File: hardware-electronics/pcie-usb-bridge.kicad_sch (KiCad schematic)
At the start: 27 parts, among them U10 24AA04T-I_OT, U3 PI7C9X440SLBFDE, Y1 ABM8-12.000MHZ-B2-T

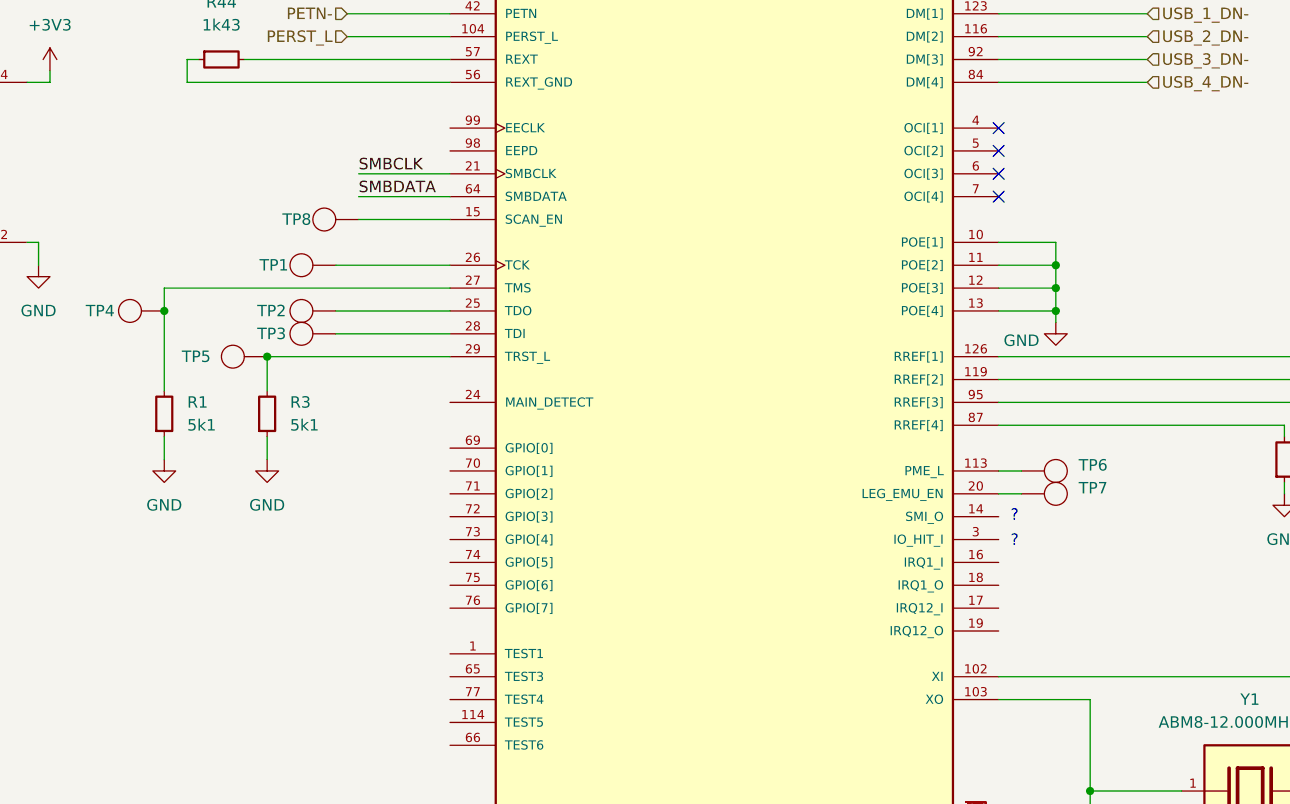
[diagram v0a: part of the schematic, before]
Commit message: [#8] SCH PCIe to USB Add TP to OHCI USB mode
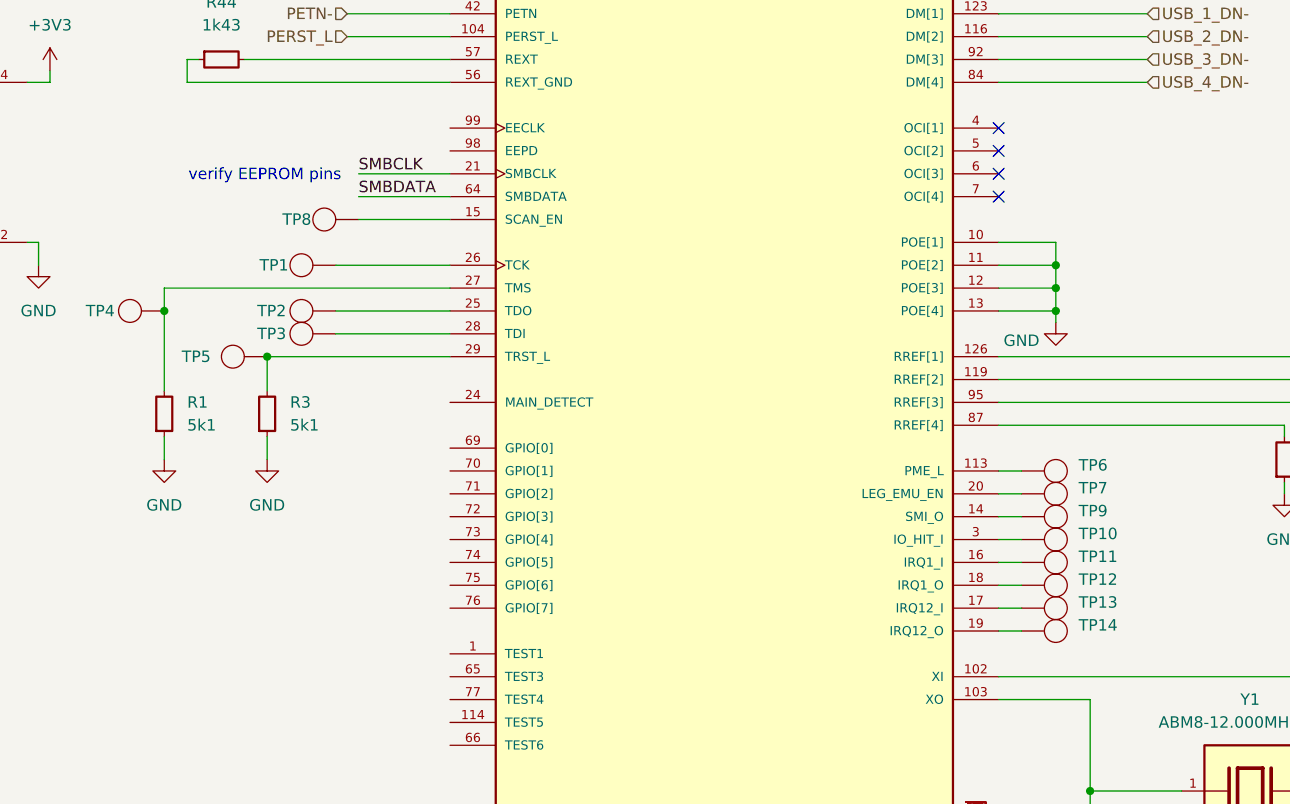
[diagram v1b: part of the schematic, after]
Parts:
- added TP10, TP11, TP12, TP13, TP14, TP9: ~, symbol M2SmartHomeSymbols:TP_SMD_1mm
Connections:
- net at U3.14 (SMI_O): now also TP9.
- net at U3.16 (IRQ1_I): now also TP11.
- net at U3.17 (IRQ12_I): now also TP13.
- net at U3.18 (IRQ1_O): now also TP12.
- net at U3.19 (IRQ12_O): now also TP14.
- net at U3.3 (IO_HIT_I): now also TP10.
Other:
- note added: "verify EEPROM pins"
- note removed: "?"

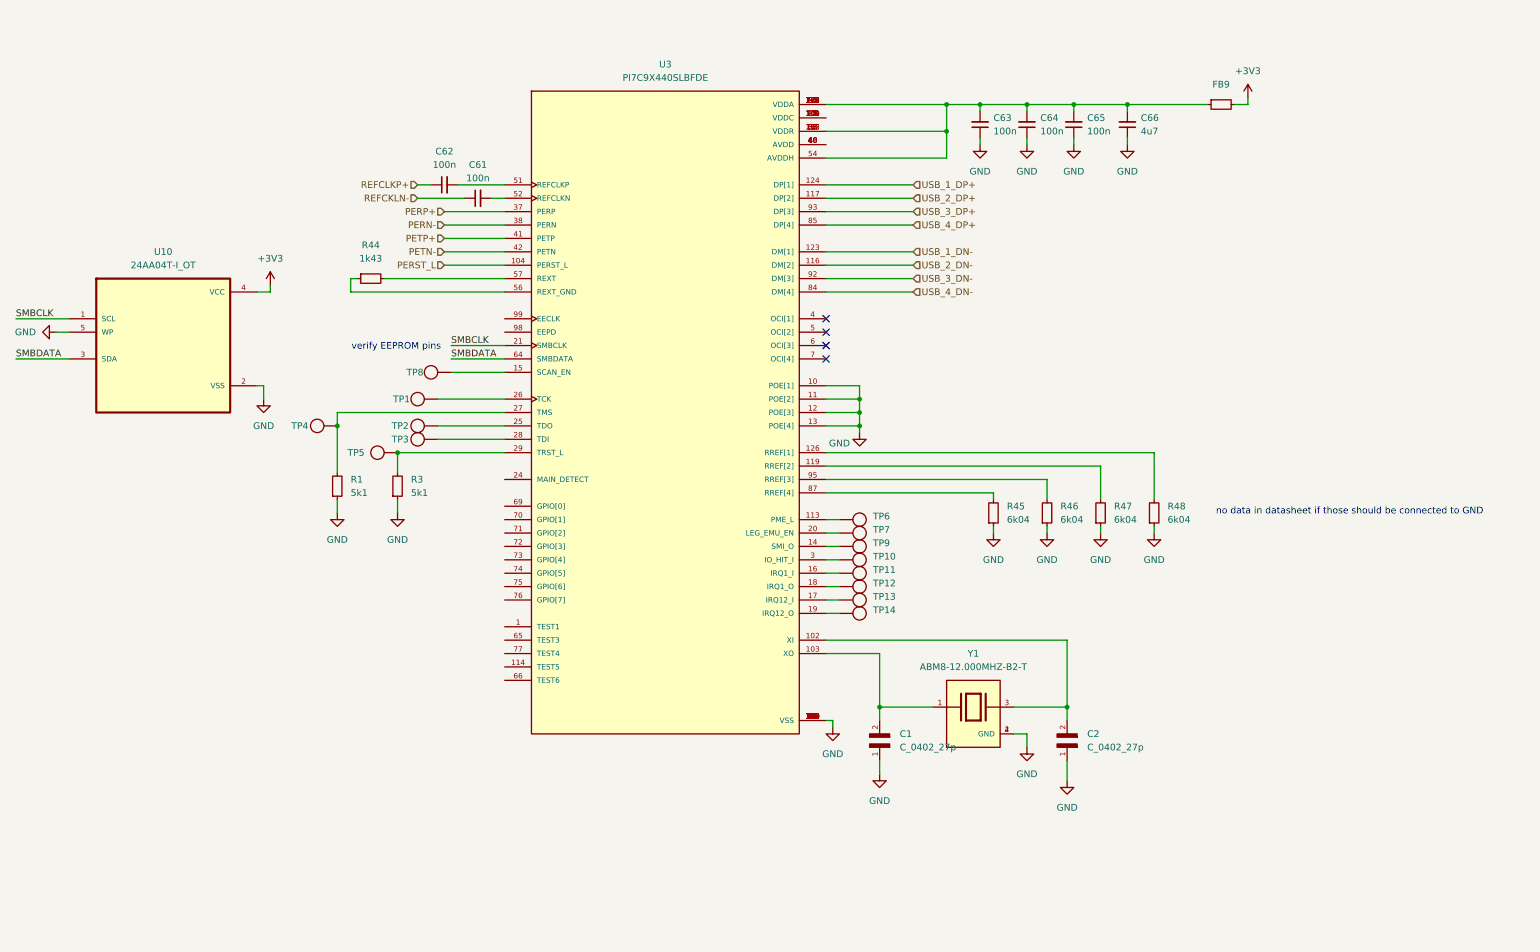
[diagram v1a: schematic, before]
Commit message: [#8] SCH PCIe to USB Connect rest of the pins
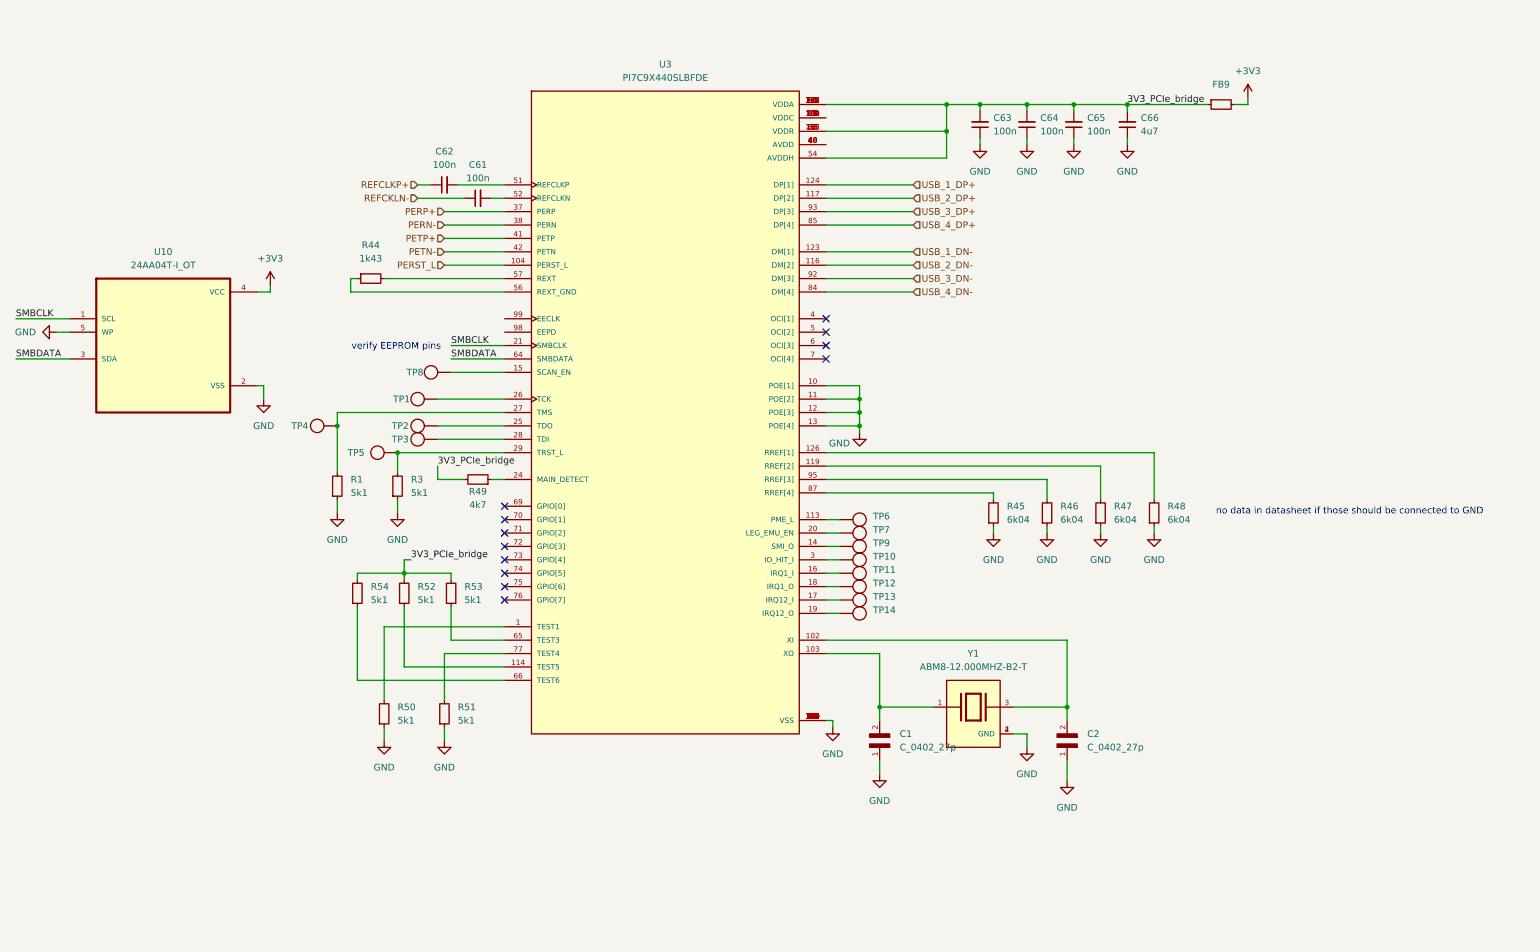
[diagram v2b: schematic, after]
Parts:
- added R49: R_4k7_0402, M2SmartHomeFootprints:R_0402, symbol M2SmartHomeSymbols:R_4k7_0402
- added R50, R51, R52, R53, R54: R_5k1_0402, R_5k1_0402:R_0402_1005Metric, symbol M2SmartHomeSymbols:R_5k1_0402
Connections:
- net GND: now also R50.1, R51.1
- net 3V3_PCIe_bridge: now reaches C63.2, C64.2, C65.2, C66.2, FB9.1, U3.105 (VDDR), U3.112 (VDDR), U3.115 (VDDA), U3.121 (VDDA), U3.122 (VDDA), U3.128 (VDDA), U3.33 (VDDR), U3.54 (AVDDH), U3.67 (VDDR), U3.8 (VDDR), U3.83 (VDDA), U3.90 (VDDA), U3.91 (VDDA), U3.97 (VDDA)
- net 3V3_PCIe_bridge: now also R49.2, R52.2, R53.2, R54.2
- net at U3.1 (TEST1): now also R50.2
- net at U3.114 (TEST5): now also R52.1
- net at U3.24 (MAIN_DETECT): now also R49.1
- net at U3.65 (TEST3): now also R53.1
- net at U3.66 (TEST6): now also R54.1
- net at U3.77 (TEST4): now also R51.2
- no-connect marks 4 -> 12

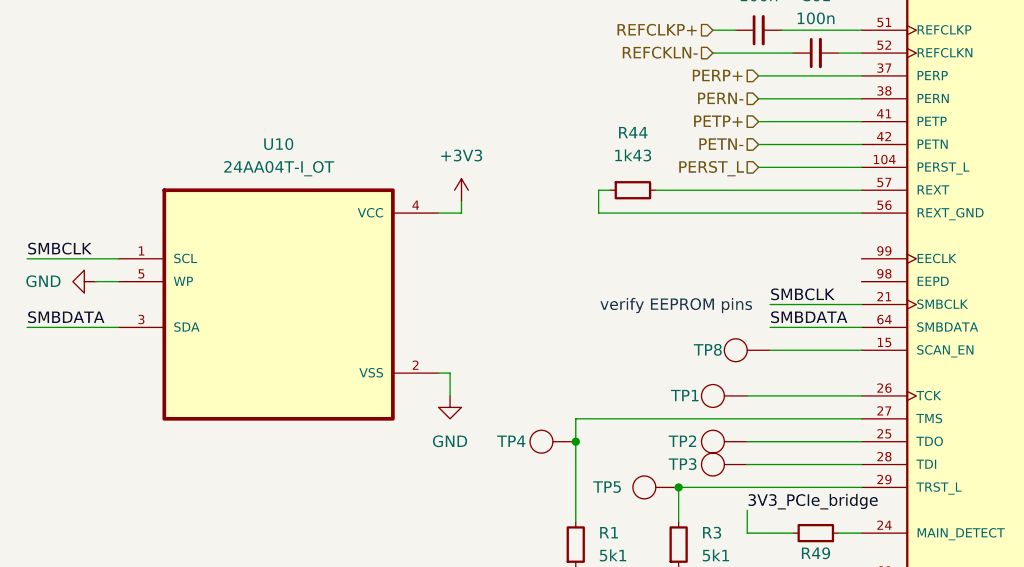
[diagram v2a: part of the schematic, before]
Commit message: [#8] SCH PCIe to USB Corrected EEPROM connections
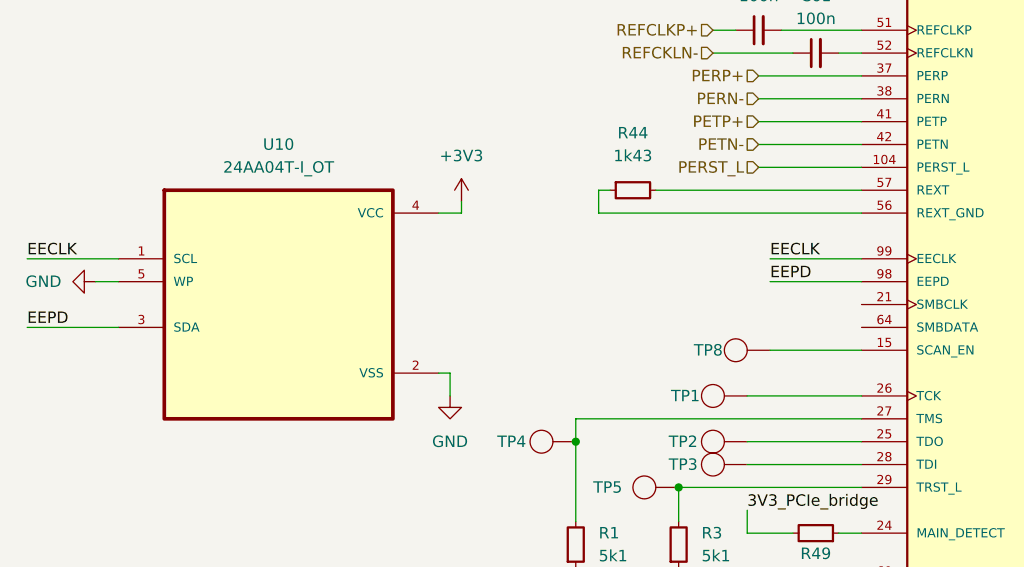
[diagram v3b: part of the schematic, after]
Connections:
- net EEPD: now reaches U3.98 (EEPD)
- net EEPD: now also U10.3 (SDA)
- net EECLK: now reaches U3.99 (EECLK)
- net EECLK: now also U10.1 (SCL)
- net SMBCLK: no longer names the net of U3.21 (SMBCLK)
- net SMBCLK: no longer U10.1 (SCL)
- net SMBDATA: no longer names the net of U3.64 (SMBDATA)
- net SMBDATA: no longer U10.3 (SDA)
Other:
- note removed: "verify EEPROM pins"

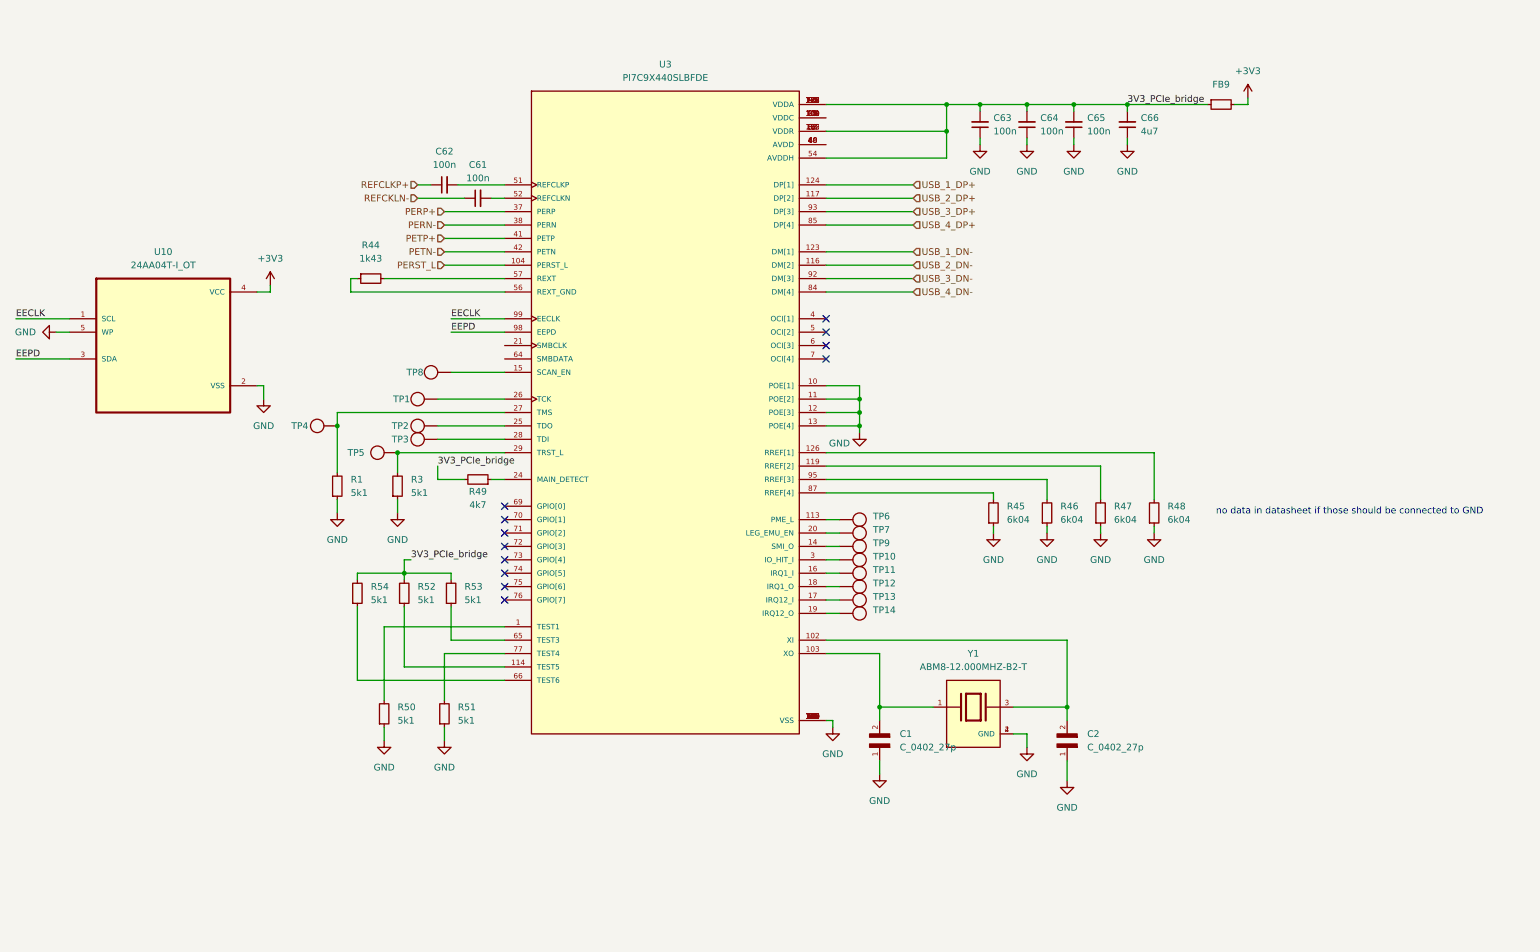
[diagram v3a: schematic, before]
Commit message: [#8] SCH PCIe to USB Add pullups on I2C lines
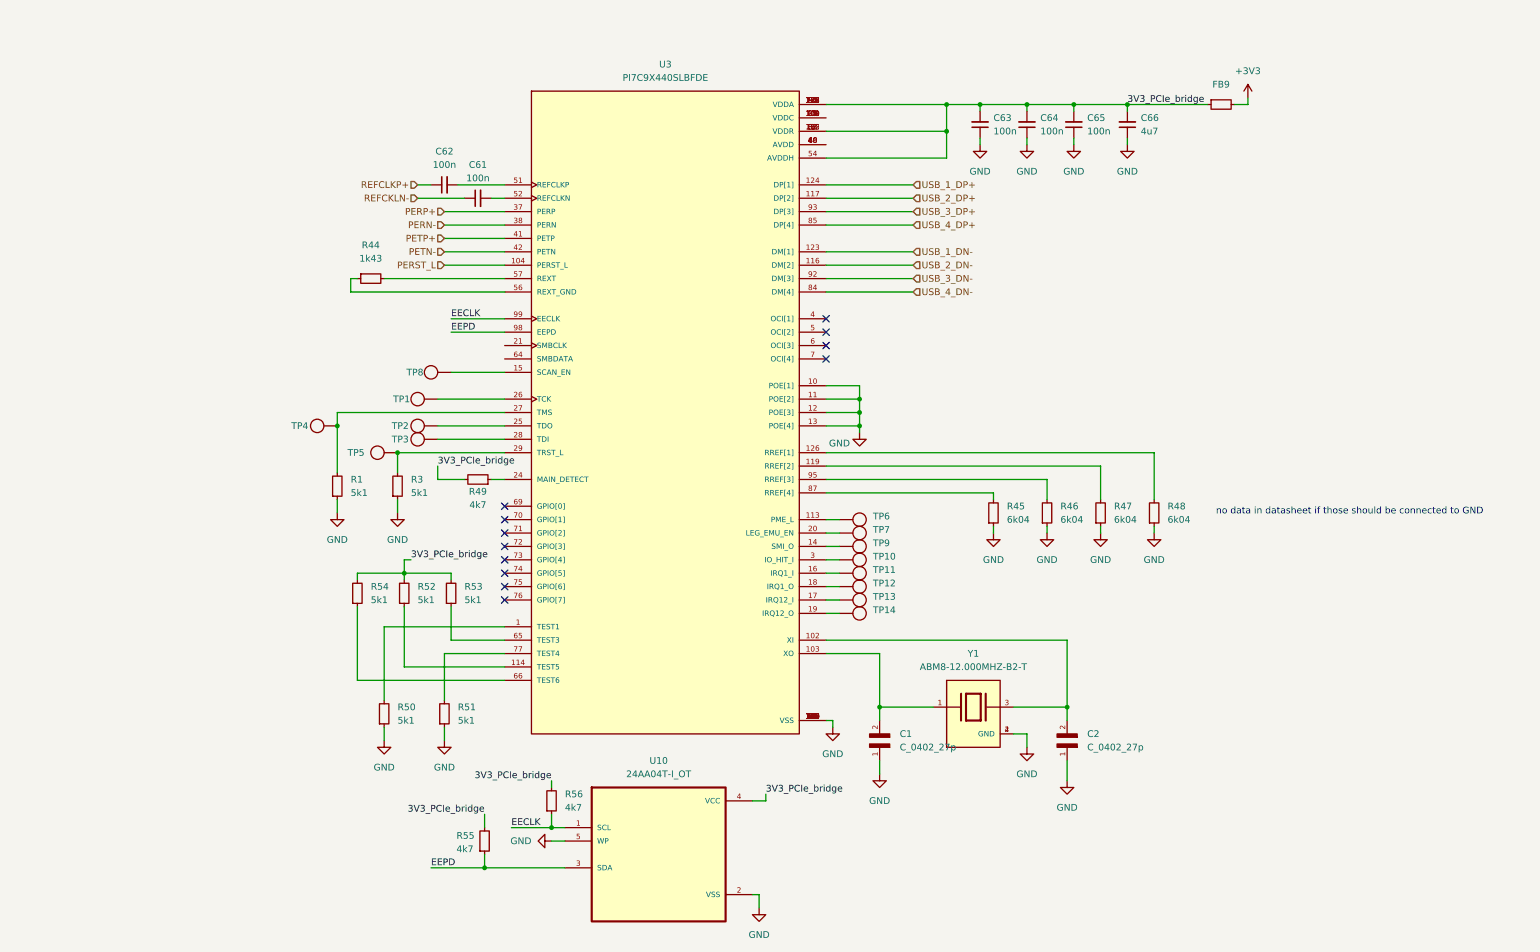
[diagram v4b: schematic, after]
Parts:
- added R55, R56: R_4k7_0402, M2SmartHomeFootprints:R_0402, symbol M2SmartHomeSymbols:R_4k7_0402
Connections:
- net +3V3: no longer U10.4 (VCC)
- net 3V3_PCIe_bridge: now also U10.4 (VCC), R55.2, R56.2
- net EECLK: now also R56.1
- net EEPD: now also R55.1
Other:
- moved on the sheet: U10
